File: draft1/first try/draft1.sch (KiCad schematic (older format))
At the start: 0 parts

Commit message: added components from aftermarket library
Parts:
- added IC? (x2): 74AVC4TD245PW,118, SOP65P640X110-16N, symbol SamacSys_Parts:74AVC4TD245PW,118
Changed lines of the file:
@@
 Comment4 ""
 $EndDescr
+$Comp
+L SamacSys_Parts:74AVC4TD245PW,118 IC?
+U 1 1 5F141984
+P 2950 4100
+F 0 "IC?" H 3600 4365 50  0000 C CNN
+F 1 "74AVC4TD245PW,118" H 3600 4274 50  0000 C CNN
+F 2 "SOP65P640X110-16N" H 4100 4200 50  0001 L CNN
+F 3 "https://assets.nexperia.com/documents/data-sheet/74AVC4TD245PW.pdf" H 4100 4100 50  0001 L CNN
+F 4 "74AVC4TD245PW - 4-bit dual supply translating transceiver with configurable voltage translation;3-state@en-us" H 4100 4000 50  0001 L CNN "Description"
+F 5 "1.1" H 4100 3900 50  0001 L CNN "Height"
+F 6 "Nexperia" H 4100 3800 50  0001 L CNN "Manufacturer_Name"
+F 7 "74AVC4TD245PW,118" H 4100 3700 50  0001 L CNN "Manufacturer_Part_Number"
+F 8 "74AVC4TD245PW,118" H 4100 3600 50  0001 L CNN "Arrow Part Number"
+F 9 "https://www.arrow.com/en/products/74avc4td245pw118/nexperia" H 4100 3500 50  0001 L CNN "Arrow Price/Stock"
+F 10 "771-74AVC4TD245PW118" H 4100 3400 50  0001 L CNN "Mouser Part Number"
+F 11 "https://www.mouser.co.uk/ProductDetail/Nexperia/74AVC4TD245PW118?qs=vbj%2FKoHZRAgBf2UMQ6EFpA%3D%3D" H 4100 3300 50  0001 L CNN "Mouser Price/Stock"
+	1    2950 4100
+	1    0    0    -1
+$EndComp
+$Comp
+L SamacSys_Parts:74AVC4TD245PW,118 IC?
+U 1 1 5F1437F5
+P 6200 4100
+F 0 "IC?" H 6850 4365 50  0000 C CNN
+F 1 "74AVC4TD245PW,118" H 6850 4274 50  0000 C CNN
+F 2 "SOP65P640X110-16N" H 7350 4200 50  0001 L CNN
+F 3 "https://assets.nexperia.com/documents/data-sheet/74AVC4TD245PW.pdf" H 7350 4100 50  0001 L CNN
+F 4 "74AVC4TD245PW - 4-bit dual supply translating transceiver with configurable voltage translation;3-state@en-us" H 7350 4000 50  0001 L CNN "Description"
+F 5 "1.1" H 7350 3900 50  0001 L CNN "Height"
+F 6 "Nexperia" H 7350 3800 50  0001 L CNN "Manufacturer_Name"
+F 7 "74AVC4TD245PW,118" H 7350 3700 50  0001 L CNN "Manufacturer_Part_Number"
+F 8 "74AVC4TD245PW,118" H 7350 3600 50  0001 L CNN "Arrow Part Number"
+F 9 "https://www.arrow.com/en/products/74avc4td245pw118/nexperia" H 7350 3500 50  0001 L CNN "Arrow Price/Stock"
+F 10 "771-74AVC4TD245PW118" H 7350 3400 50  0001 L CNN "Mouser Part Number"
+F 11 "https://www.mouser.co.uk/ProductDetail/Nexperia/74AVC4TD245PW118?qs=vbj%2FKoHZRAgBf2UMQ6EFpA%3D%3D" H 7350 3300 50  0001 L CNN "Mouser Price/Stock"
+	1    6200 4100
+	1    0    0    -1
+$EndComp
 $EndSCHEMATC

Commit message: added connector
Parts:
- added J?: Conn_01x24, symbol Connector_Generic:Conn_01x24
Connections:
- net labels added: +VBAT, ASC_EXT_OVER33, ASC_IN_33, ASC_LOAD_33, ASC_OUT33, ASC_PHI1_33, ASC_PHI2_33, GND, HARD_RESET_33, LF_CLK_33
- wire segments 0 -> 26
- no-connect marks 0 -> 12

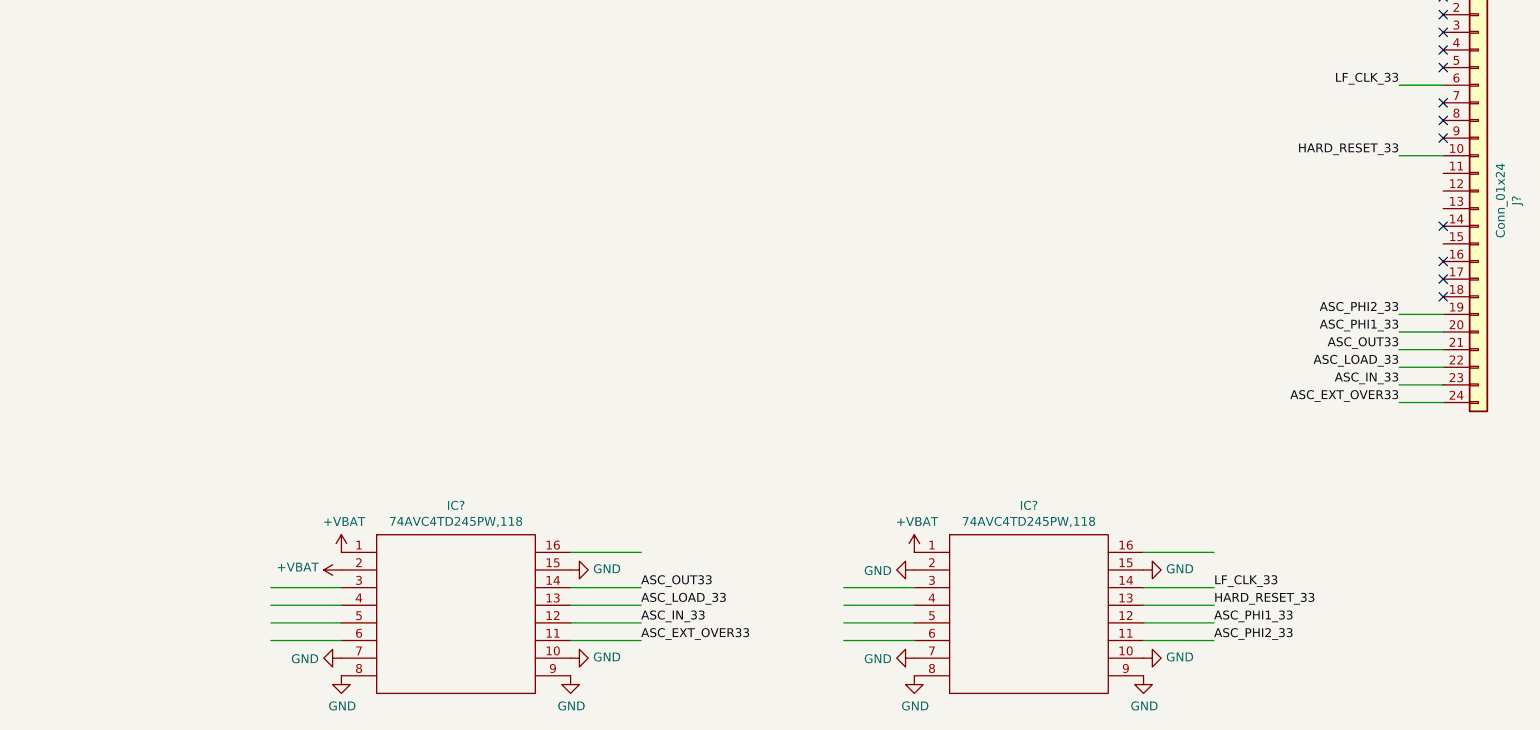
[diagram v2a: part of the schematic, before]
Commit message: added power flags
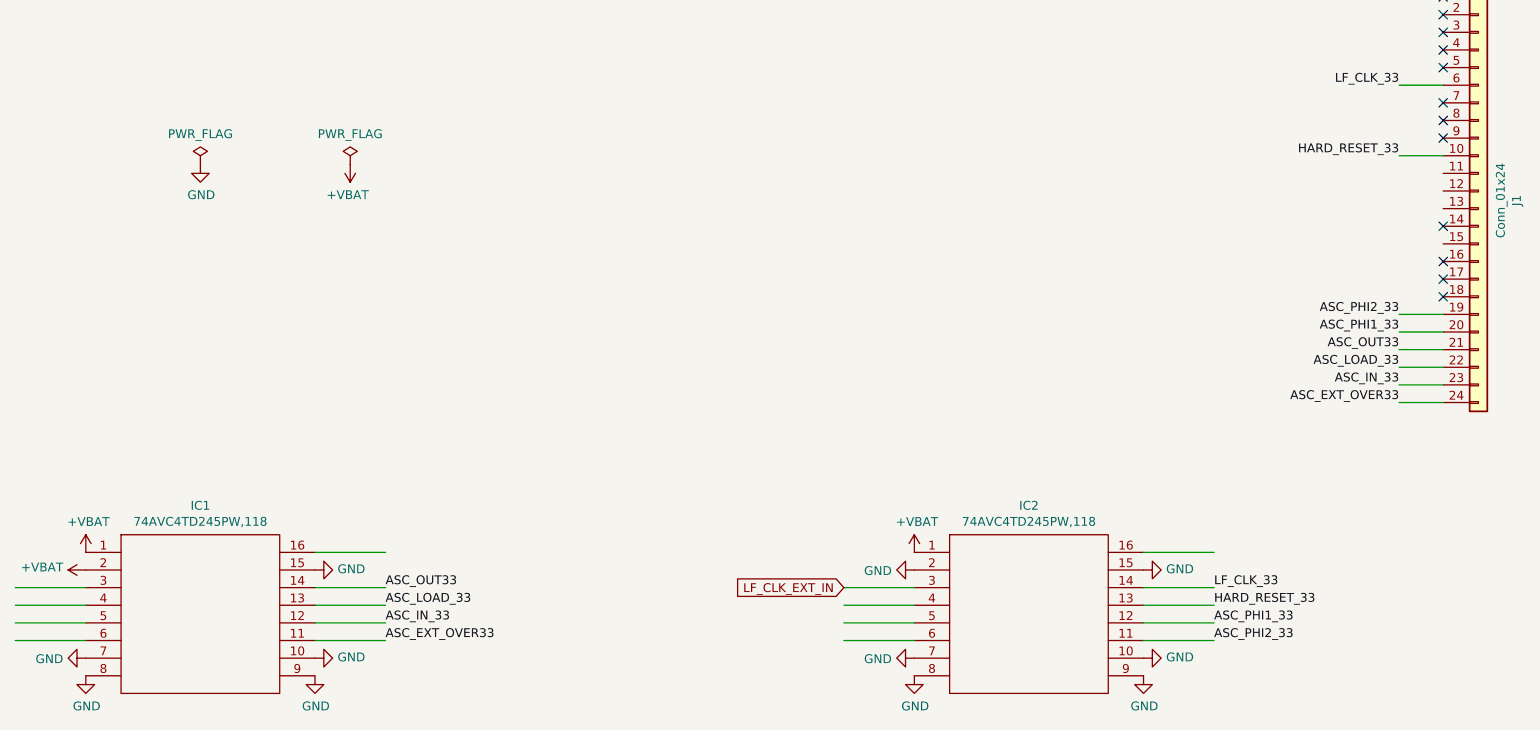
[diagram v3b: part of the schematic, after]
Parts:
- gave numbers to parts that had none: 3
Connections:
- net labels added: LF_CLK_EXT_IN
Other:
- moved on the sheet: IC1

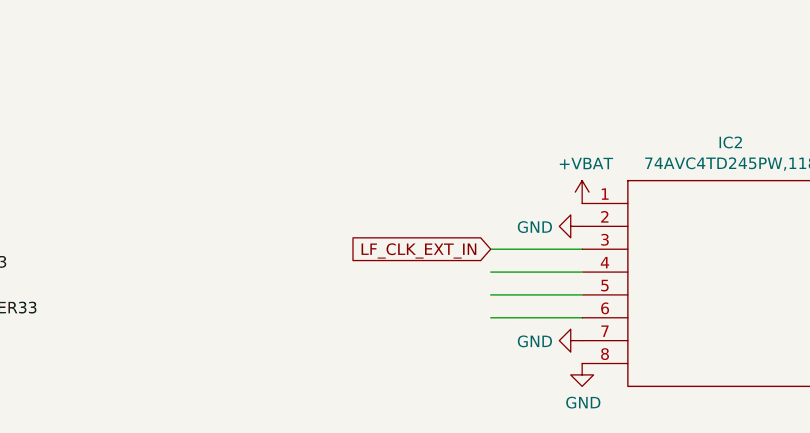
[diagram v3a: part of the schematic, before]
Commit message: added some global labels
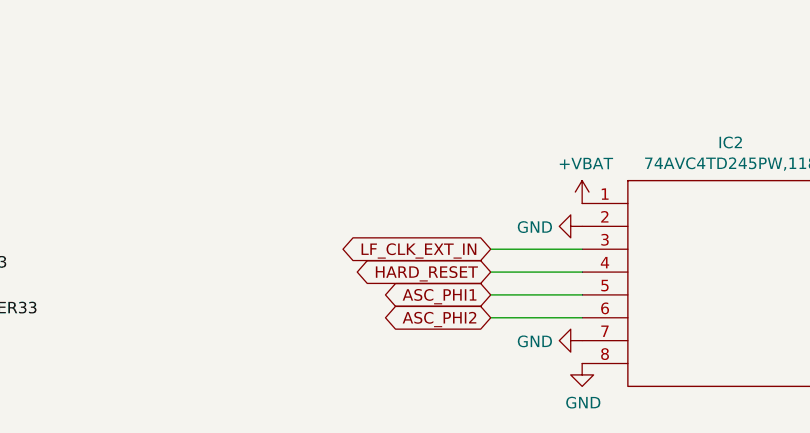
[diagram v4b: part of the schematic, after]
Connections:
- net labels added: ASC_PHI1, ASC_PHI2, HARD_RESET
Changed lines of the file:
@@
 	-1   0    0    1
 $EndComp
-Text GLabel 5800 4300 0    50   Input ~ 0
+Text GLabel 5800 4300 0    50   BiDi ~ 0
 LF_CLK_EXT_IN
+Text GLabel 5800 4400 0    50   BiDi ~ 0
+HARD_RESET
+Text GLabel 5800 4500 0    50   BiDi ~ 0
+ASC_PHI1
+Text GLabel 5800 4600 0    50   BiDi ~ 0
+ASC_PHI2
 $EndSCHEMATC

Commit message: added new sheet
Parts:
- added R7: NP, Resistor_SMD:R_0603_1608Metric, symbol Device:R_US
- added R8: 100k, Resistor_SMD:R_0603_1608Metric, symbol Device:R_US
- IC1, IC2: footprint SOP65P640X110-16N -> SamacSys_Parts:SOP65P640X110-16N
- J1: footprint (none) -> Connector_PinHeader_2.54mm:PinHeader_1x24_P2.54mm_Vertical
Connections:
- net labels added: +UART33, 3WB_CLK, 3WB_DATA, 3WB_ENB, ASC_EXT_OVERRIDE, ASC_IN, ASC_LOAD, ASC_OUT, HR
- wire segments 26 -> 34
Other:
- moved on the sheet: IC1

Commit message: added scum pad to sch, made VDDIO pin
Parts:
- added P?: SCUM_PAD, symbol draft1library:SCUM_PAD
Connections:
- net +VBAT: now also P?.26 (VBAT)
- net GND: now also P?.27 (GND)
- new net GPIO0: P?.28 (GPIO0)
- new net GPIO1: P?.29 (GPIO1)
- new net GPIO10: P?.39 (GPIO10)
- new net GPIO11: P?.40 (GPIO11)
- new net GPIO12: P?.41 (GPIO12)
- new net GPIO13: P?.42 (GPIO13)
- new net GPIO14: P?.43 (GPIO14)
- new net GPIO15: P?.44 (GPIO15)
- new net GPIO2: P?.30 (GPIO2)
- new net GPIO3: P?.31 (GPIO3)
- new net GPIO4: P?.32 (GPIO4)
- new net GPIO5: P?.33 (GPIO5)
- new net GPIO6: P?.34 (GPIO6)
- new net GPIO7: P?.35 (GPIO7)
- new net GPIO8: P?.37 (GPIO8)
- new net GPIO9: P?.38 (GPIO9)
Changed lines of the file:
@@
 F1 "scumpadsheet.sch" 50
 $EndSheet
+$Comp
+L draft1library:SCUM_PAD P?
+U 1 1 5F2FDF4D
+P 18650 3750
+F 0 "P?" H 22178 3513 50  0000 L CNN
+F 1 "SCUM_PAD" H 22178 3422 50  0000 L CNN
+F 2 "" H 18650 3750 50  0001 C CNN
+F 3 "" H 18650 3750 50  0001 C CNN
+	1    18650 3750
+	1    0    0    -1
+$EndComp
+$Comp
+L draft1library:+VBAT #PWR?
+U 1 1 5F2FF5C2
+P 15650 7350
+F 0 "#PWR?" H 15650 7200 50  0001 C CNN
+F 1 "+VBAT" H 15665 7523 50  0000 C CNN
+F 2 "" H 15650 7350 50  0001 C CNN
+F 3 "" H 15650 7350 50  0001 C CNN
+	1    15650 7350
+	-1   0    0    1
+$EndComp
+Wire Wire Line
+	15650 7050 15650 7350
+$Comp
+L power:GND #PWR?
+U 1 1 5F303554
+P 15850 7350
+F 0 "#PWR?" H 15850 7100 50  0001 C CNN
+F 1 "GND" V 15855 7222 50  0000 R CNN
+F 2 "" H 15850 7350 50  0001 C CNN
+F 3 "" H 15850 7350 50  0001 C CNN
+	1    15850 7350
+	1    0    0    -1
+$EndComp
+Wire Wire Line
+	15850 7050 15850 7350
+Text GLabel 16600 7050 3    50   BiDi ~ 0
+GPIO0
+Text GLabel 16750 7050 3    50   BiDi ~ 0
+GPIO1
+Text GLabel 16900 7050 3    50   BiDi ~ 0
+GPIO2
+Text GLabel 17050 7050 3    50   BiDi ~ 0
+GPIO3
+Text GLabel 17200 7050 3    50   BiDi ~ 0
+GPIO4
+Text GLabel 17350 7050 3    50   BiDi ~ 0
+GPIO5
+Text GLabel 17500 7050 3    50   BiDi ~ 0
+GPIO6
+Text GLabel 17650 7050 3    50   BiDi ~ 0
+GPIO7
+Text GLabel 17950 7050 3    50   BiDi ~ 0
+GPIO8
+Text GLabel 18100 7050 3    50   BiDi ~ 0
+GPIO9
+Text GLabel 18250 7050 3    50   BiDi ~ 0
+GPIO10
+Text GLabel 18400 7050 3    50   BiDi ~ 0
+GPIO11
+Text GLabel 18550 7050 3    50   BiDi ~ 0
+GPIO12
+Text GLabel 18700 7050 3    50   BiDi ~ 0
+GPIO13
+Text GLabel 18850 7050 3    50   BiDi ~ 0
+GPIO14
+Text GLabel 19000 7050 3    50   BiDi ~ 0
+GPIO15
+$Comp
+L power:PWR_FLAG #FLG?
+U 1 1 5F308B79
+P 1050 1850
+F 0 "#FLG?" H 1050 1925 50  0001 C CNN
+F 1 "PWR_FLAG" H 1050 2023 50  0000 C CNN
+F 2 "" H 1050 1850 50  0001 C CNN
+F 3 "~" H 1050 1850 50  0001 C CNN
+	1    1050 1850
+	1    0    0    -1
+$EndComp
 $EndSCHEMATC

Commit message: added some pins
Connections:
- net +VDDIO: now reaches P?.36 (VDDIO)
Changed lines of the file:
@@
 	1    0    0    -1
 $EndComp
+$Comp
+L draft1library:+VDDIO #PWR?
+U 1 1 5F30D677
+P 17800 7350
+F 0 "#PWR?" H 17800 7200 50  0001 C CNN
+F 1 "+VDDIO" H 17815 7523 50  0000 C CNN
+F 2 "" H 17800 7350 50  0001 C CNN
+F 3 "" H 17800 7350 50  0001 C CNN
+	1    17800 7350
+	-1   0    0    1
+$EndComp
+Wire Wire Line
+	17800 7050 17800 7350
 $EndSCHEMATC

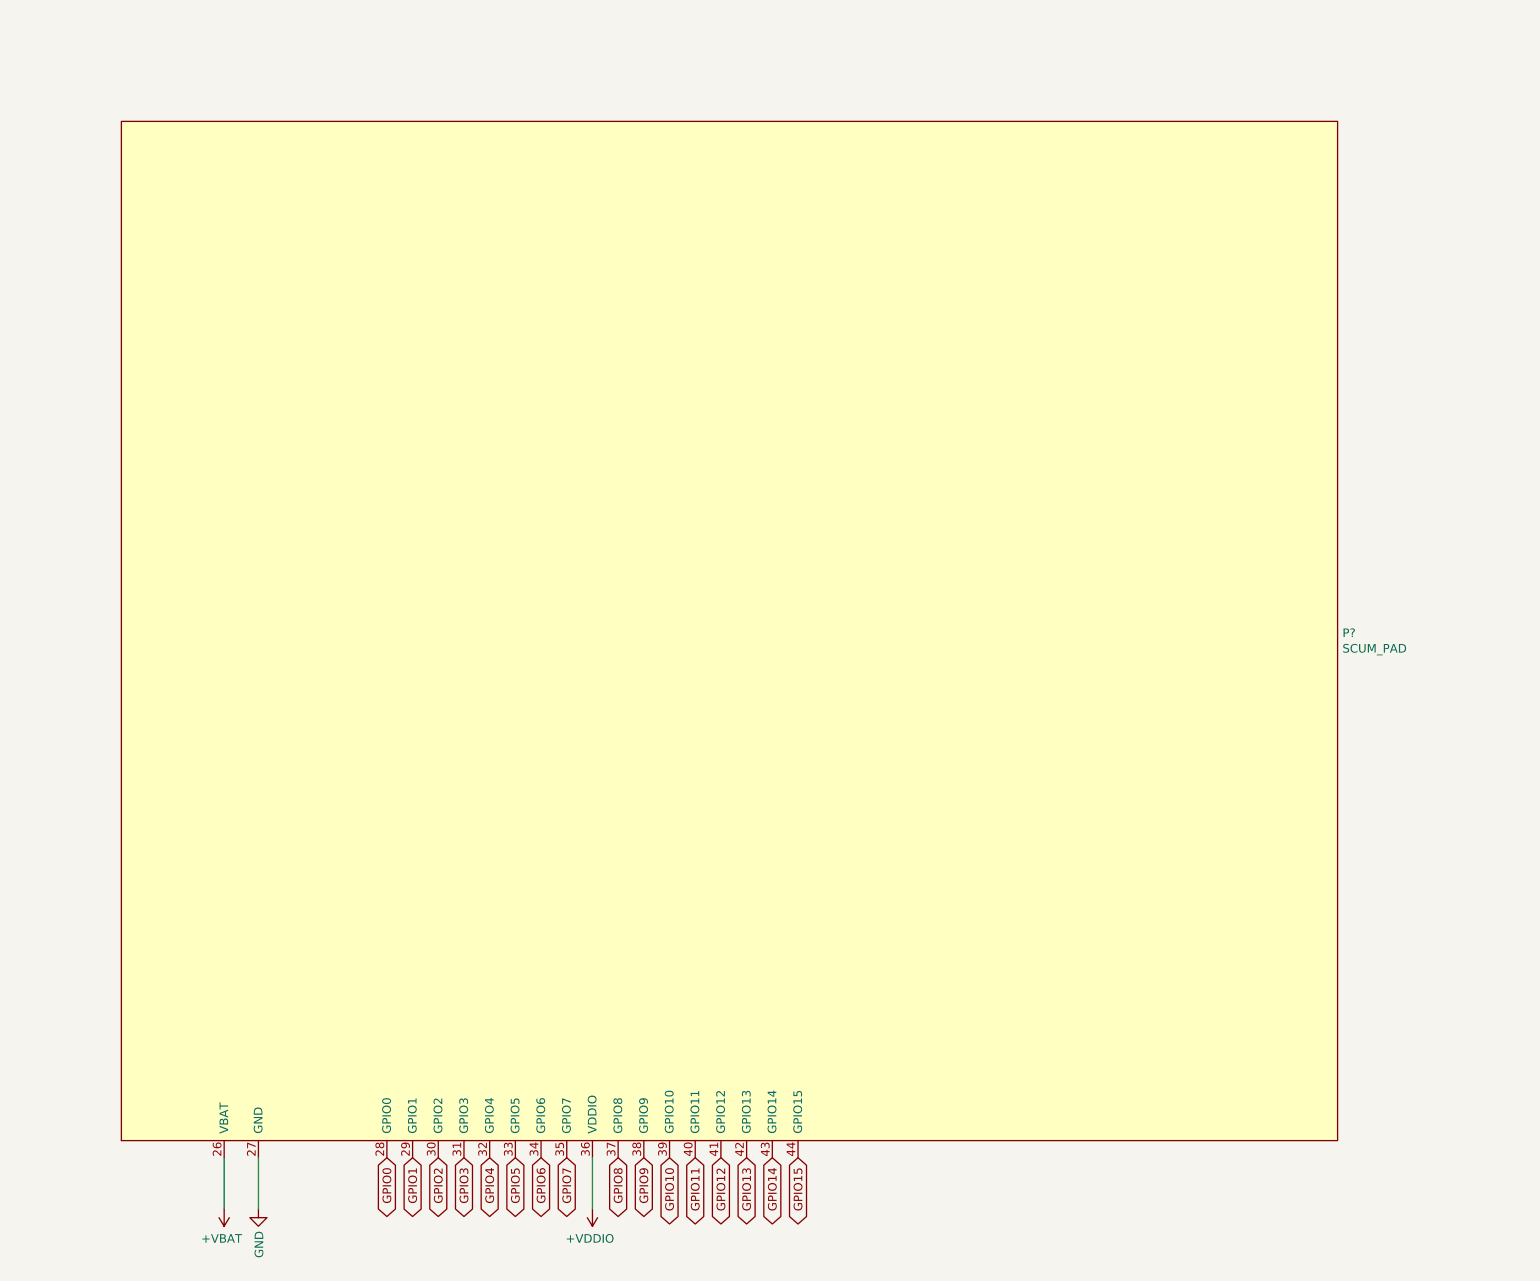
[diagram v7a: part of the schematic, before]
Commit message: added all pins to scum pad
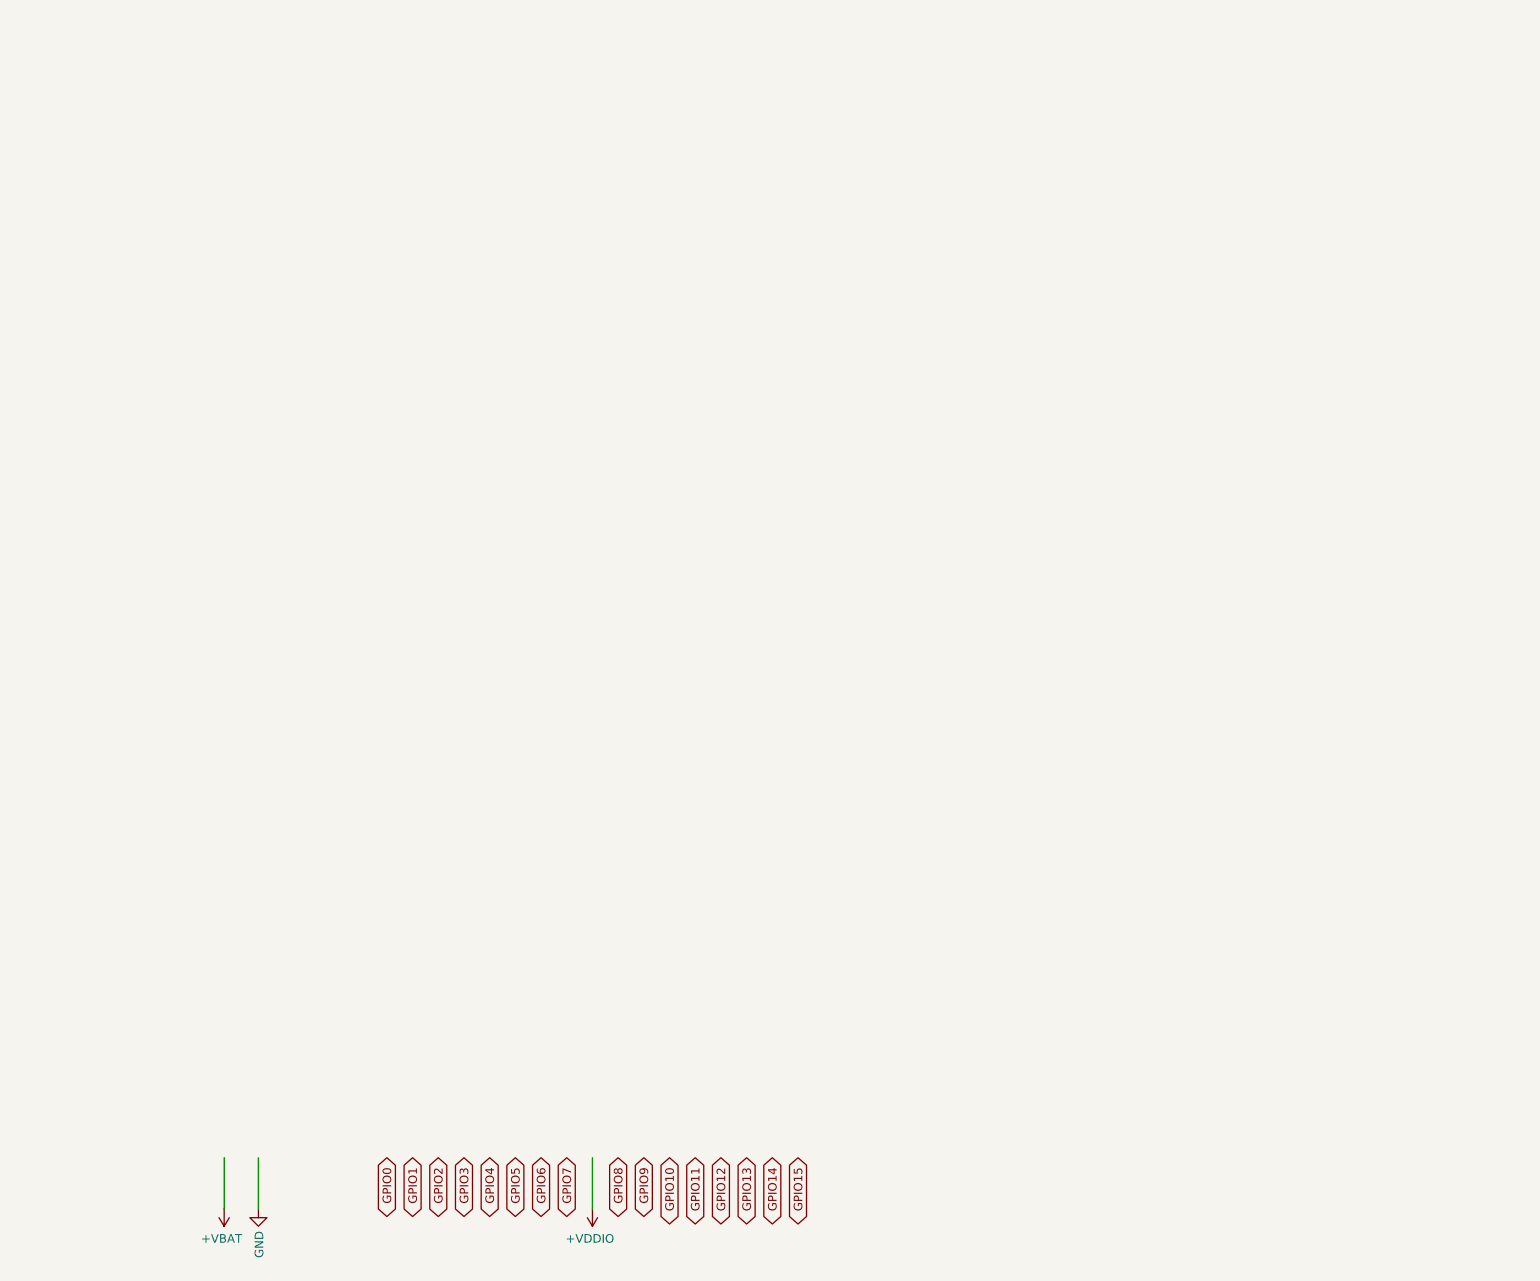
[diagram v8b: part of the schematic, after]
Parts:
- removed P?: SCUM_PAD, symbol draft1library:SCUM_PAD
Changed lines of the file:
@@
 	-1   0    0    1
-$EndComp
-$Sheet
-S 12300 0    12650 8500
-U 5F1F2002
-F0 "scumpadsheet" 50
-F1 "scumpadsheet.sch" 50
-$EndSheet
-$Comp
-L draft1library:SCUM_PAD P?
-U 1 1 5F2FDF4D
-P 18650 3750
-F 0 "P?" H 22178 3513 50  0000 L CNN
-F 1 "SCUM_PAD" H 22178 3422 50  0000 L CNN
-F 2 "" H 18650 3750 50  0001 C CNN
-F 3 "" H 18650 3750 50  0001 C CNN
-	1    18650 3750
-	1    0    0    -1
 $EndComp
 $Comp
@@
 Wire Wire Line
 	17800 7050 17800 7350
+$Sheet
+S 12300 0    12650 8500
+U 5F1F2002
+F0 "scumpadsheet" 50
+F1 "scumpadsheet.sch" 50
+$EndSheet
 $EndSCHEMATC
